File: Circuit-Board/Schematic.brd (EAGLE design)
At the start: 34 x 48.9 mm, 17 parts, among them Q1 MOSFET-NCHANNEL2N7000, U1 DS1631U+

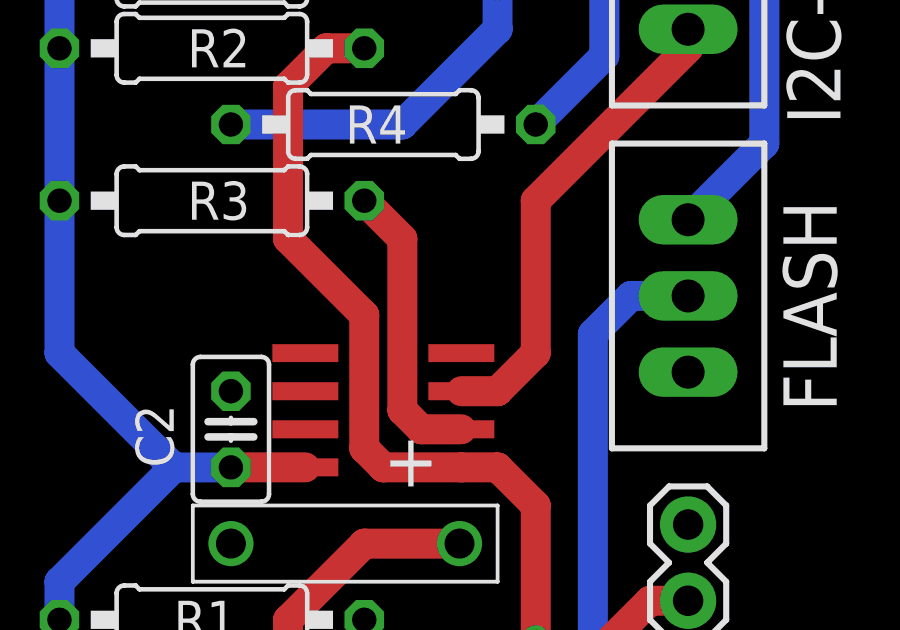
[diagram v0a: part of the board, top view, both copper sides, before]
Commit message: Updated circuit board
Major error in circuit board design with second switch going to Tout
instead of SCK on the DS1361.
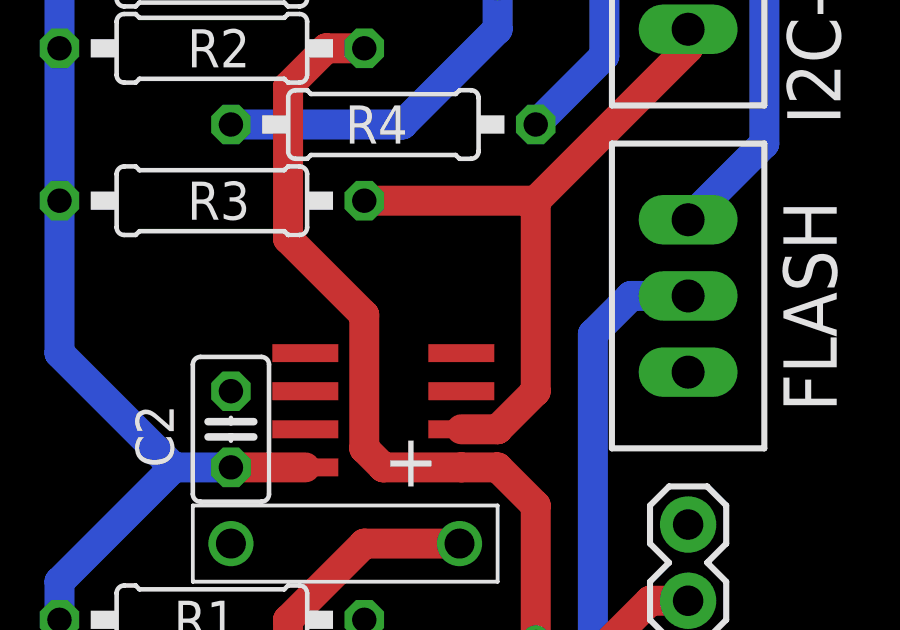
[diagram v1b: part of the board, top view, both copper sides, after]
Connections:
- removed net N$3: R3.1, U1.2
- net N$9: now also R3.1, U1.2; no longer U1.3
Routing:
- net N$3: track 9.74 -> 0.00 mm
- net N$9: track 15.9 -> 22.9 mm
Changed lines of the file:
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@@
 <contactref element="RELAY" pad="1"/>
-</signal>
-<signal name="N$3">
-<contactref element="U1" pad="2"/>
-<contactref element="R3" pad="1"/>
-<wire x1="15.875" y1="27.94" x2="17.145" y2="26.67" width="1" layer="1"/>
-<wire x1="17.145" y1="26.67" x2="17.145" y2="20.955" width="1" layer="1"/>
-<wire x1="17.145" y1="20.955" x2="17.78" y2="20.32" width="1" layer="1"/>
-<wire x1="17.78" y1="20.32" x2="19.11" y2="20.32" width="1" layer="1"/>
 </signal>
 <signal name="N$4">
@@
 <signal name="N$9">
 <contactref element="I2C-RELAY" pad="1"/>
-<contactref element="U1" pad="3"/>
-<wire x1="19.11" y1="21.59" x2="20.32" y2="21.59" width="1" layer="1"/>
-<wire x1="20.32" y1="21.59" x2="21.59" y2="22.86" width="1" layer="1"/>
-<wire x1="21.59" y1="22.86" x2="21.59" y2="27.94" width="1" layer="1"/>
+<contactref element="R3" pad="1"/>
+<contactref element="U1" pad="2"/>
+<wire x1="15.875" y1="27.94" x2="21.59" y2="27.94" width="1" layer="1"/>
 <wire x1="21.59" y1="27.94" x2="26.67" y2="33.02" width="1" layer="1"/>
 <wire x1="26.67" y1="33.02" x2="26.67" y2="33.655" width="1" layer="1"/>
+<wire x1="19.11" y1="20.32" x2="20.32" y2="20.32" width="1" layer="1"/>
+<wire x1="20.32" y1="20.32" x2="21.59" y2="21.59" width="1" layer="1"/>
+<wire x1="21.59" y1="21.59" x2="21.59" y2="27.94" width="1" layer="1"/>
 </signal>
 <signal name="N$13">
